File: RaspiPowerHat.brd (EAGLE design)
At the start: 62.2 x 43.6 mm, 28 parts, among them U2 Value, U3 LM25011MYX/NOPB, X1 RASPI_GPIO_B+#_PIN

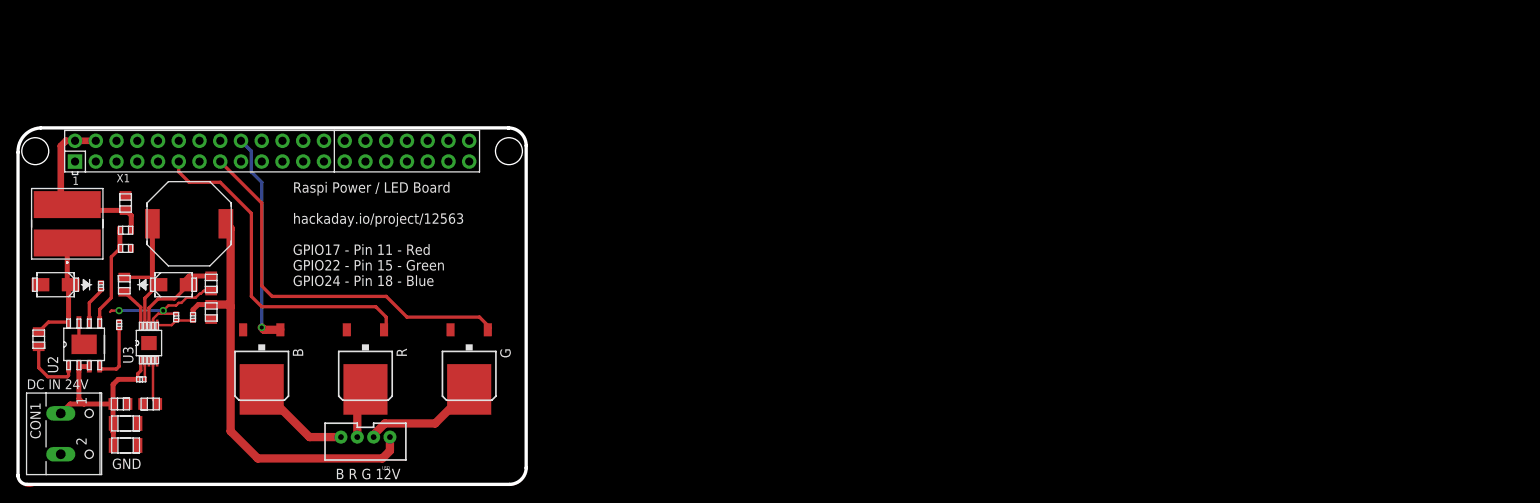
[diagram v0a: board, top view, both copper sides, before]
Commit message: Added another RGB channel, fixed footprints
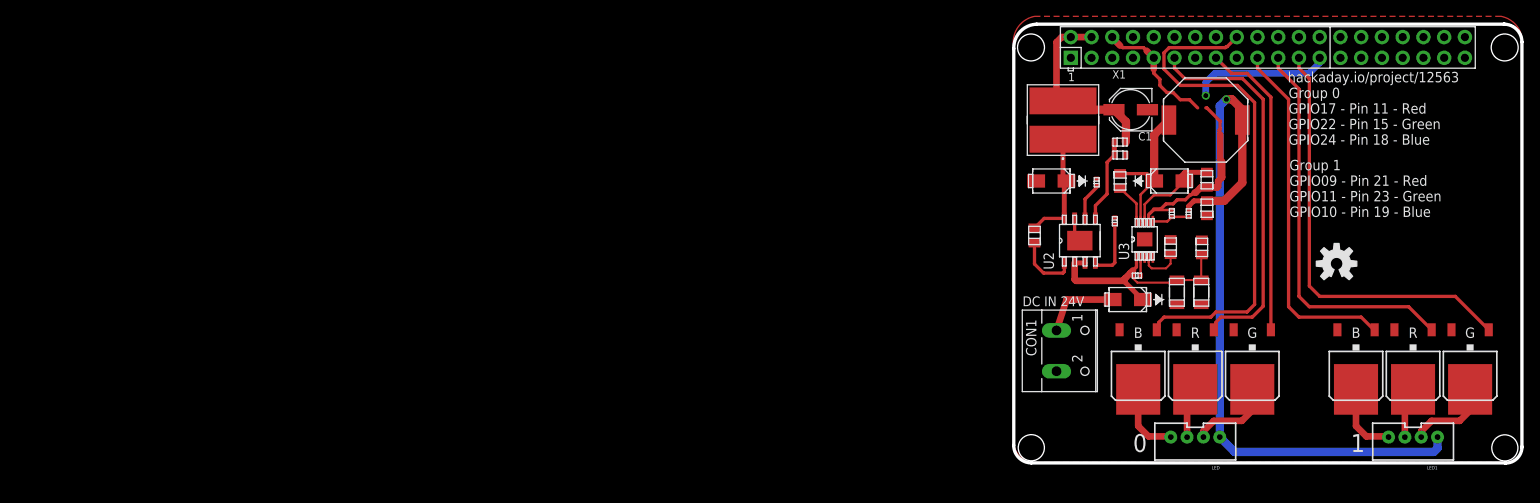
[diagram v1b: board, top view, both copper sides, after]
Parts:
- removed B, G, R: NTD4906N, transistor-power:D-PAK_TO252AA
- added BLUE, BLUE2, GREEN, GREEN2, RED, RED2: NTD4906N, transistor-power:D-PAK_TO252AA
- added C1: (no value), rcl:PANASONIC_C
- added LED1: (no value), SparkFun-Connectors:JST-4-PTH-VERT
- added U$21: (no value), SparkFun-Aesthetics:OSHW-LOGO-M
- U$15: value 16SVPC39MV -> B360A-13-F; device TI-LMR14050SSDA:GEN_CAP -> TI-LMR14050SSDA:SMA
- moved U$1 133.8 mm to (159.6, 45.4), turned to 90 degrees
- moved U$4 133.0 mm to (159.5, 39.9), turned to 270 degrees
- moved U$18 129.7 mm to (156.5, 39.9), turned to 270 degrees
- moved U$3 126.4 mm to (155.7, 45.4), turned to 90 degrees
- moved U$8 125.1 mm to (160.0, 61.0)
- moved U$15 123.3 mm to (150.5, 39.0), turned to 180 degrees
- moved U$19 122.6 mm to (155.9, 49.5)
- moved U$20 122.6 mm to (160.2, 50.2)
- moved U$7 122.6 mm to (160.2, 53.7)
- moved U$9 122.6 mm to (158.0, 49.5)
- moved U$10 122.6 mm to (139.1, 46.8)
- moved U$11 122.6 mm to (142.6, 61.0)
- moved U$12 122.6 mm to (141.1, 53.5)
- moved U$16 122.6 mm to (146.7, 53.3)
- moved U$17 122.6 mm to (148.9, 48.6)
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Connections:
- removed net GPIO17: R.1, X1.11
- removed net GPIO22: G.1, X1.15
- removed net GPIO24: B.1, X1.18
- new net BLUE1: BLUE.1, X1.18
- new net BLUE2: BLUE2.4, LED1.4
- new net GREEN1: GREEN.1, X1.15
- new net GREEN2: GREEN2.4, LED1.2
- new net INBLUE2: BLUE2.1, X1.19
- new net INGREEN2: GREEN2.1, X1.23
- new net INRED2: RED2.1, X1.21
- new net N$2: CON1.1, U$15.2
- new net RED1: RED.1, X1.11
- new net RED2: LED1.3, RED2.4
- net 12V: now also LED1.1
- net 24VIN: now also U$15.1; no longer CON1.1
- net 5V: now also C1.+; no longer U$15.1
- net BLUE: now also BLUE.4; no longer B.4
- net GND: now also BLUE.3, BLUE2.3, C1.-, GREEN.3, GREEN2.3, RED.3, RED2.3; no longer B.3, G.3, R.3, U$15.2
- net GREEN: now also GREEN.4; no longer G.4
- net RED: now also RED.4; no longer R.4
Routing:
- net BLUE1: track 0.00 -> 62.5 mm
- net INGREEN2: track 0.00 -> 52.7 mm
- net GND: track 20.3 -> 70.9 mm, vias 2 -> 1
- net INRED2: track 0.00 -> 48.2 mm
- net GPIO22: track 47.8 -> 0.00 mm
- net RED1: track 0.00 -> 46.3 mm
- net INBLUE2: track 0.00 -> 43.8 mm
- net GPIO17: track 41.6 -> 0.00 mm
- net GREEN1: track 0.00 -> 37.2 mm
- net 12V: track 54.1 -> 90.3 mm, vias 0 -> 1
- net GPIO24: track 26.3 -> 0.00 mm, vias 1 -> 0
- net GREEN2: track 0.00 -> 13.3 mm
- net BLUE2: track 0.00 -> 10.9 mm
- net N$2: track 0.00 -> 9.61 mm
- net RED2: track 0.00 -> 6.99 mm
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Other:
- board size 62.2 x 43.6 mm -> 62.2 x 53.7 mm
- board text added: "0"
- board text added: "1"
- board text added: "B"
- board text added: "C:/Users/bench_000/Desktop/Unicorn.bmp"
- board text added: "G"
- board text added: "Group 0 GPIO17 - Pin 11 - Red GPIO22 - Pin 15 - Green GPIO24 - Pin 18 - Blue"
- board text added: "Group 1 GPIO09 - Pin 21 - Red GPIO11 - Pin 23 - Green GPIO10 - Pin 19 - Blue"
- board text added: "R"
- board text removed: "B R G 12V"
- board text removed: "GND"
- board text removed: "GPIO17 - Pin 11 - Red GPIO22 - Pin 15 - Green GPIO24 - Pin 18 - Blue"
- board text removed: "Raspi Power / LED Board"
